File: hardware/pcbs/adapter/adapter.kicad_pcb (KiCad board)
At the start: 2 copper layers, 13.4 x 10.8 mm, 2 parts, among them J1 Conn_01x04_Pin, J2 XLR4

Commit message: chore: finalize v6c production run
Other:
- board text added: "af 25"
- board text removed: "af 25 inside"
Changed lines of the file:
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@@
 		(layer "Edge.Cuts")
 	)
-	(gr_text "af 25\ninside"
+	(gr_text "af 25"
 		(at 145.826708 109.029669 90)
 		(layer "F.SilkS")

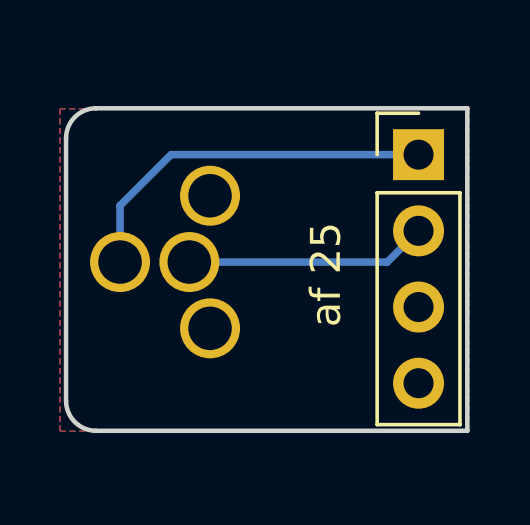
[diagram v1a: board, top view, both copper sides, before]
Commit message: feat: update to 5-pin XLR for sleep
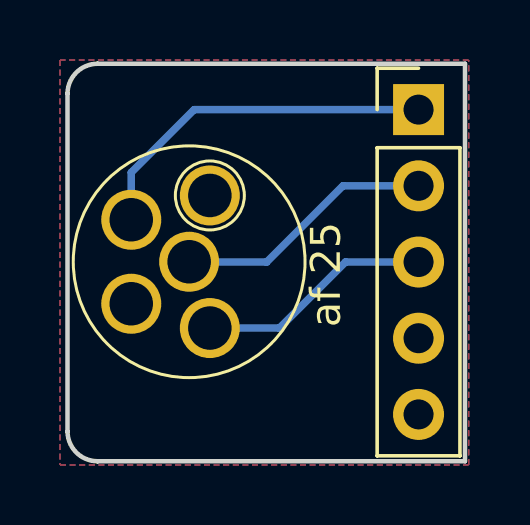
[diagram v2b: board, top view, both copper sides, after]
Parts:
- removed J2: XLR4, connector_audio:MiniXLR-4_Rean_RT4MPR
- added J3: Conn_01x05_Pin, Connector_PinHeader_2.54mm:PinHeader_1x05_P2.54mm_Vertical, F.Cu at (148.3, 101.8)
- J1: value Conn_01x04_Pin -> XLR5; footprint Connector_PinHeader_2.54mm:PinHeader_1x04_P2.54mm_Vertical -> connector_audio:MiniXLR-5_Rean_RT5MPR
- moved J1 8.44 mm to (140.7, 106.8), turned to -90 degrees
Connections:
- J1 pad 1: /TC+ -> /GND
- J1 pad 2: /DET -> /TC+
- J1 pad 3: /GND -> /HEATER
- J1 pad 4: /HEATER -> /SLP
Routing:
- net /SLP: track 0.00 -> 7.87 mm
- net /DET: track 8.07 -> 8.69 mm
- net /TC+: track 12.5 -> 12.0 mm
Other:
- board size 13.4 x 10.8 mm -> 13.2 x 13.2 mm

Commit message: feat: hw v7a
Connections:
- net /GND renamed /BLUE
- net /HEATER renamed /RED
- net /SLP renamed /GREEN
- net /TC+ renamed /SLP_EXT
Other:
- board text added: "af 25 v7a"
- board text removed: "af 25"
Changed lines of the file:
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@@
 	(paper "A4")
 	(title_block
-		(title "MiniXLR adapter")
-		(date "2025-08-18")
-		(rev "6c")
+		(title "MiniXLR adapter (main)")
+		(date "2025-11-10")
+		(rev "7a")
 		(company "elagil")
 	)
@@
 	)
 	(net 0 "")
-	(net 1 "/TC+")
+	(net 1 "/RED")
 	(net 2 "/DET")
-	(net 3 "/GND")
-	(net 4 "/HEATER")
-	(net 5 "/SLP")
+	(net 3 "/BLUE")
+	(net 4 "/SLP_EXT")
+	(net 5 "/GREEN")
 	(footprint "connector_audio:MiniXLR-5_Rean_RT5MPR"
 		(layer "F.Cu")
@@
 			(layers "*.Cu" "*.Mask")
 			(remove_unused_layers no)
-			(net 3 "/GND")
+			(net 3 "/BLUE")
 			(pinfunction "P1")
 			(pintype "passive")
@@
 			(layers "*.Cu" "*.Mask")
 			(remove_unused_layers no)
-			(net 1 "/TC+")
+			(net 4 "/SLP_EXT")
 			(pinfunction "P2")
 			(pintype "passive")
@@
 			(layers "*.Cu" "*.Mask")
 			(remove_unused_layers no)
-			(net 4 "/HEATER")
+			(net 1 "/RED")
 			(pinfunction "P3")
 			(pintype "passive")
@@
 			(layers "*.Cu" "*.Mask")
 			(remove_unused_layers no)
-			(net 5 "/SLP")
+			(net 5 "/GREEN")
 			(pinfunction "P3")
 			(pintype "passive")
@@
 			(layers "*.Cu" "*.Mask")
 			(remove_unused_layers no)
-			(net 1 "/TC+")
+			(net 4 "/SLP_EXT")
 			(pinfunction "Pin_1")
 			(pintype "passive")
@@
 			(layers "*.Cu" "*.Mask")
 			(remove_unused_layers no)
-			(net 5 "/SLP")
+			(net 5 "/GREEN")
 			(pinfunction "Pin_3")
 			(pintype "passive")
@@
 			(layers "*.Cu" "*.Mask")
 			(remove_unused_layers no)
-			(net 3 "/GND")
+			(net 3 "/BLUE")
 			(pinfunction "Pin_4")
 			(pintype "passive")
@@
 			(layers "*.Cu" "*.Mask")
 			(remove_unused_layers no)
-			(net 4 "/HEATER")
+			(net 1 "/RED")
 			(pinfunction "Pin_5")
 			(pintype "passive")
@@
 		(layer "Edge.Cuts")
 	)
-	(gr_text "af 25"
-		(at 145.826708 109.029669 90)
-		(layer "F.SilkS")
+	(gr_text "af 25\nv7a"
+		(at 143.5 112.75 -90)
+		(layer "B.SilkS")
 		(effects
 			(font
@@
 				(thickness 0.15)
 			)
-			(justify left bottom)
-		)
-	)
-	(segment
-		(start 140.846 101.779)
-		(end 148.326708 101.779)
-		(width 0.25)
-		(layer "B.Cu")
-		(net 1)
-	)
-	(segment
-		(start 138.75 103.875)
-		(end 140.846 101.779)
-		(width 0.25)
-		(layer "B.Cu")
-		(net 1)
-	)
-	(segment
-		(start 138.75 105.45)
-		(end 138.75 103.875)
-		(width 0.25)
-		(layer "B.Cu")
-		(net 1)
+			(justify left bottom mirror)
+		)
 	)
 	(segment
@@
 	)
 	(segment
+		(start 140.846 101.779)
+		(end 148.326708 101.779)
+		(width 0.25)
+		(layer "B.Cu")
+		(net 4)
+	)
+	(segment
+		(start 138.75 103.875)
+		(end 140.846 101.779)
+		(width 0.25)
+		(layer "B.Cu")
+		(net 4)
+	)
+	(segment
+		(start 138.75 105.45)
+		(end 138.75 103.875)
+		(width 0.25)
+		(layer "B.Cu")
+		(net 4)
+	)
+	(segment
 		(start 145.891 106.859)
 		(end 143.69 109.06)
@@
 	)
 	(zone
-		(net 4)
-		(net_name "/HEATER")
+		(net 1)
+		(net_name "/RED")
 		(layer "F.Cu")
 		(hatch edge 0.5)
@@
 	(zone
 		(net 3)
-		(net_name "/GND")
+		(net_name "/BLUE")
 		(layer "B.Cu")
 		(hatch edge 0.5)
